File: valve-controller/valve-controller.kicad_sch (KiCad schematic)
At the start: 1 part

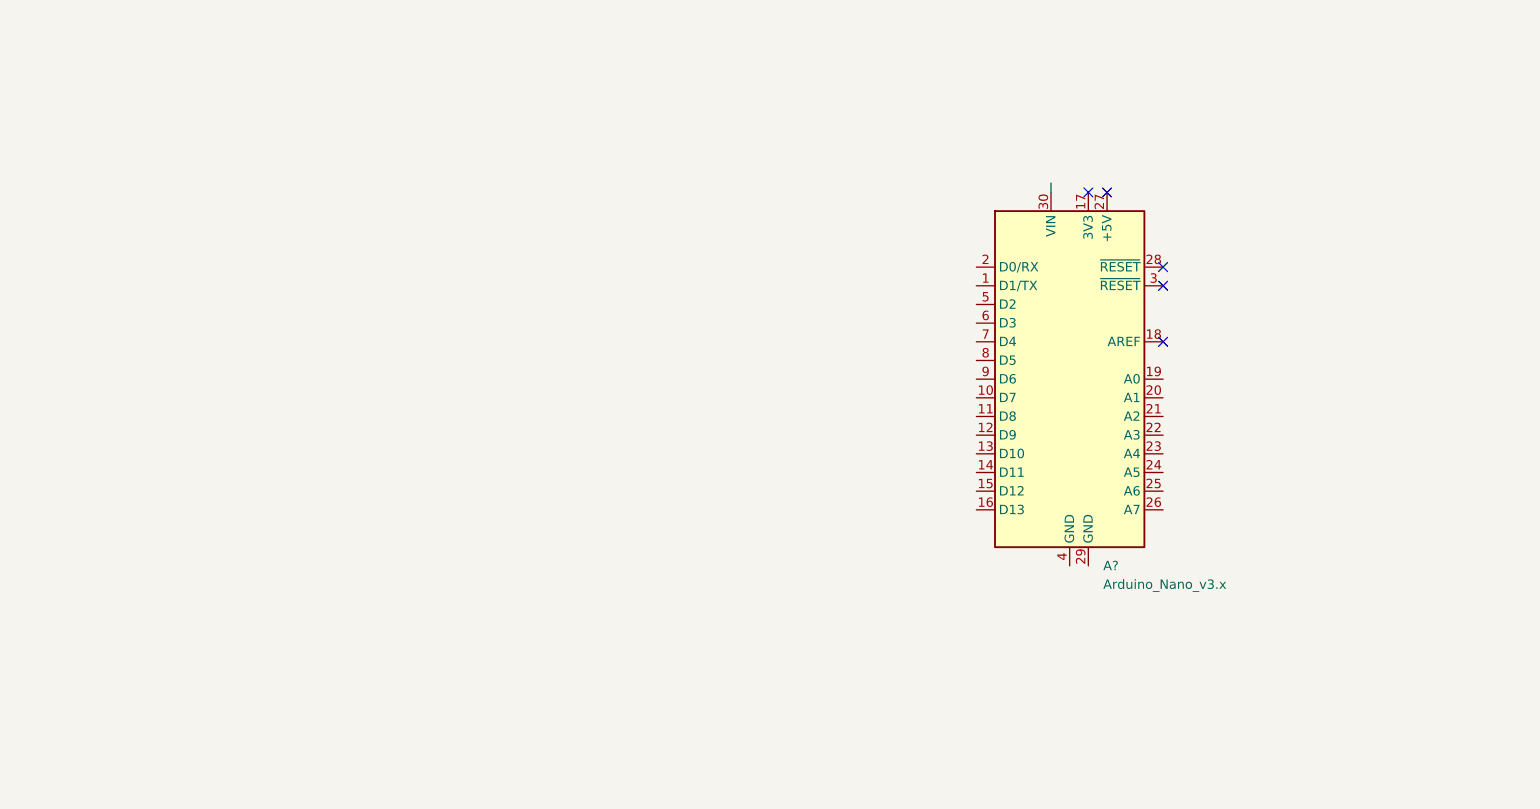
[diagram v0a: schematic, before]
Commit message: making wiring diagram for valve controller
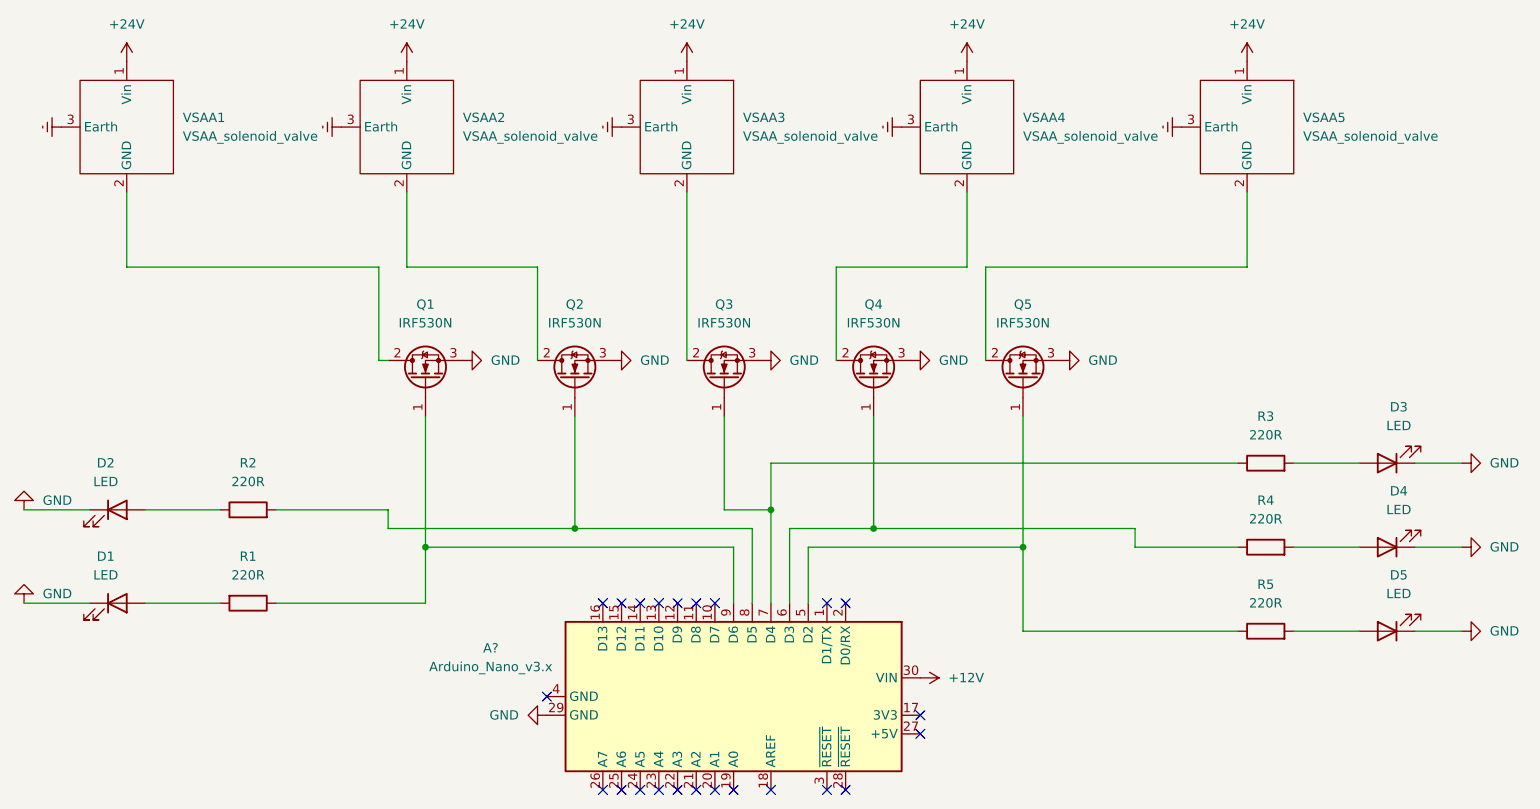
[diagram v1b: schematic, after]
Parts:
- added D1, D2, D3, D4, D5: LED, symbol Device:LED
- added Q1, Q2, Q3, Q4, Q5: IRF530N, symbol Transistor_FET:IRF540N
- added R1, R2, R3, R4, R5: 220R, symbol Device:R
- added VSAA1, VSAA2, VSAA3, VSAA4, VSAA5: VSAA_solenoid_valve, symbol my_library:VSAA_solenoid_valve
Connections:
- net GND: now reaches A?.29 (GND)
- net GND: now also D1.1 (K), D2.1 (K), D3.1 (K), D4.1 (K), D5.1 (K), Q1.3 (S), Q2.3 (S), Q3.3 (S), Q4.3 (S), Q5.3 (S)
- net +12V: now reaches A?.30 (VIN)
- net at A?.5 (D2): now also Q5.1 (G), R5.1
- net at A?.6 (D3): now also Q4.1 (G), R4.1
- net at A?.7 (D4): now also Q3.1 (G), R3.1
- net at A?.8 (D5): now also Q2.1 (G), R2.2
- net at A?.9 (D6): now also Q1.1 (G), R1.1
- new net: Q2.2 (D), VSAA2.2 (GND)
- new net: D5.2 (A), R5.2
- new net: D4.2 (A), R4.2
- new net: Q1.2 (D), VSAA1.2 (GND)
- new net: D1.2 (A), R1.2
- new net: Q3.2 (D), VSAA3.2 (GND)
- new net: D3.2 (A), R3.2
- new net: Q5.2 (D), VSAA5.2 (GND)
- new net: D2.2 (A), R2.1
- new net: Q4.2 (D), VSAA4.2 (GND)
- new net +24V: VSAA1.1 (Vin), VSAA2.1 (Vin), VSAA3.1 (Vin), VSAA4.1 (Vin), VSAA5.1 (Vin)
- new net Earth: VSAA1.3 (Earth), VSAA2.3 (Earth), VSAA3.3 (Earth), VSAA4.3 (Earth), VSAA5.3 (Earth)
- no-connect marks 5 -> 23
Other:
- title: (none) -> Valve controller
- moved on the sheet: A?

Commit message: change valves and transistors order
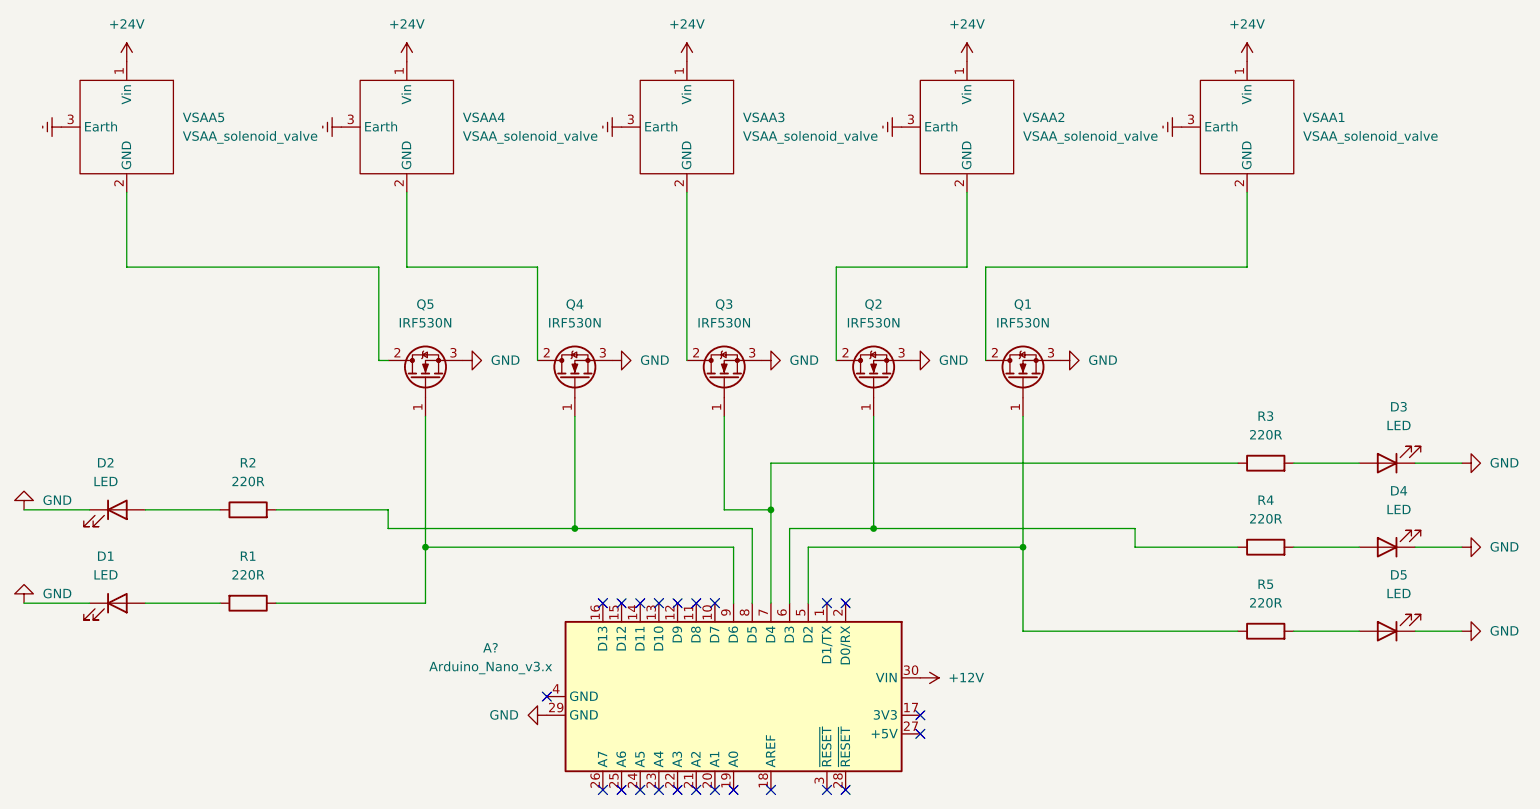
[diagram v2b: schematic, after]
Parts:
- renumbered Q5 to Q1, Q4 to Q2, Q2 to Q4, Q1 to Q5, VSAA5 to VSAA1, VSAA4 to VSAA2, VSAA2 to VSAA4, VSAA1 to VSAA5
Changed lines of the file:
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@@
   (symbol (lib_id "my_library:VSAA_solenoid_valve") (at 104.14 57.15 270) (unit 1)
     (in_bom yes) (on_board yes) (fields_autoplaced)
-    (property "Reference" "VSAA2" (id 0) (at 111.76 55.8799 90)
+    (property "Reference" "VSAA4" (id 0) (at 111.76 55.8799 90)
       (effects (font (size 1.27 1.27)) (justify left))
     )
@@
   (symbol (lib_id "Transistor_FET:IRF540N") (at 106.68 91.44 90) (unit 1)
     (in_bom yes) (on_board yes) (fields_autoplaced)
-    (property "Reference" "Q1" (id 0) (at 106.68 81.28 90))
+    (property "Reference" "Q5" (id 0) (at 106.68 81.28 90))
     (property "Value" "IRF530N" (id 1) (at 106.68 83.82 90))
     (property "Footprint" "" (id 2) (at 108.585 85.09 0)
@@
   (symbol (lib_id "Transistor_FET:IRF540N") (at 187.96 91.44 90) (unit 1)
     (in_bom yes) (on_board yes) (fields_autoplaced)
-    (property "Reference" "Q5" (id 0) (at 187.96 81.28 90))
+    (property "Reference" "Q1" (id 0) (at 187.96 81.28 90))
     (property "Value" "IRF530N" (id 1) (at 187.96 83.82 90))
     (property "Footprint" "" (id 2) (at 189.865 85.09 0)
@@
   (symbol (lib_id "my_library:VSAA_solenoid_valve") (at 66.04 57.15 270) (unit 1)
     (in_bom yes) (on_board yes) (fields_autoplaced)
-    (property "Reference" "VSAA1" (id 0) (at 73.66 55.8799 90)
+    (property "Reference" "VSAA5" (id 0) (at 73.66 55.8799 90)
       (effects (font (size 1.27 1.27)) (justify left))
     )
@@
   (symbol (lib_id "my_library:VSAA_solenoid_valve") (at 218.44 57.15 270) (unit 1)
     (in_bom yes) (on_board yes) (fields_autoplaced)
-    (property "Reference" "VSAA5" (id 0) (at 226.06 55.8799 90)
+    (property "Reference" "VSAA1" (id 0) (at 226.06 55.8799 90)
       (effects (font (size 1.27 1.27)) (justify left))
     )
@@
   (symbol (lib_id "my_library:VSAA_solenoid_valve") (at 180.34 57.15 270) (unit 1)
     (in_bom yes) (on_board yes) (fields_autoplaced)
-    (property "Reference" "VSAA4" (id 0) (at 187.96 55.8799 90)
+    (property "Reference" "VSAA2" (id 0) (at 187.96 55.8799 90)
       (effects (font (size 1.27 1.27)) (justify left))
     )
@@
   (symbol (lib_id "Transistor_FET:IRF540N") (at 127 91.44 90) (unit 1)
     (in_bom yes) (on_board yes) (fields_autoplaced)
-    (property "Reference" "Q2" (id 0) (at 127 81.28 90))
+    (property "Reference" "Q4" (id 0) (at 127 81.28 90))
     (property "Value" "IRF530N" (id 1) (at 127 83.82 90))
     (property "Footprint" "" (id 2) (at 128.905 85.09 0)
@@
   (symbol (lib_id "Transistor_FET:IRF540N") (at 167.64 91.44 90) (unit 1)
     (in_bom yes) (on_board yes) (fields_autoplaced)
-    (property "Reference" "Q4" (id 0) (at 167.64 81.28 90))
+    (property "Reference" "Q2" (id 0) (at 167.64 81.28 90))
     (property "Value" "IRF530N" (id 1) (at 167.64 83.82 90))
     (property "Footprint" "" (id 2) (at 169.545 85.09 0)
@@
       (reference "D5") (unit 1) (value "LED") (footprint "")
     )
-    (path "/1af4c67a-c000-4054-9b8f-ffb2d0e44f70"
+    (path "/9bc83bcc-e0b8-4105-9061-2c6d0758e3b7"
       (reference "Q1") (unit 1) (value "IRF530N") (footprint "")
     )
-    (path "/e3f7b2b1-9086-4943-bca4-ed77cb19a3fe"
+    (path "/e5157e2c-6aed-4c9a-ba37-76b5bf465b5a"
       (reference "Q2") (unit 1) (value "IRF530N") (footprint "")
     )
@@
       (reference "Q3") (unit 1) (value "IRF530N") (footprint "")
     )
-    (path "/e5157e2c-6aed-4c9a-ba37-76b5bf465b5a"
+    (path "/e3f7b2b1-9086-4943-bca4-ed77cb19a3fe"
       (reference "Q4") (unit 1) (value "IRF530N") (footprint "")
     )
-    (path "/9bc83bcc-e0b8-4105-9061-2c6d0758e3b7"
+    (path "/1af4c67a-c000-4054-9b8f-ffb2d0e44f70"
       (reference "Q5") (unit 1) (value "IRF530N") (footprint "")
     )
@@
       (reference "R5") (unit 1) (value "220R") (footprint "")
     )
-    (path "/b6927a09-a2f9-4c72-8b2d-0ddfde6db60a"
+    (path "/bb0bd072-604b-4f94-b7a8-ba7be997d4aa"
       (reference "VSAA1") (unit 1) (value "VSAA_solenoid_valve") (footprint "")
     )
-    (path "/05de500d-1161-4310-8519-b2804cb3777b"
+    (path "/db5ca4ae-4770-4ea2-82b0-b4805117d6f8"
       (reference "VSAA2") (unit 1) (value "VSAA_solenoid_valve") (footprint "")
     )
@@
       (reference "VSAA3") (unit 1) (value "VSAA_solenoid_valve") (footprint "")
     )
-    (path "/db5ca4ae-4770-4ea2-82b0-b4805117d6f8"
+    (path "/05de500d-1161-4310-8519-b2804cb3777b"
       (reference "VSAA4") (unit 1) (value "VSAA_solenoid_valve") (footprint "")
     )
-    (path "/bb0bd072-604b-4f94-b7a8-ba7be997d4aa"
+    (path "/b6927a09-a2f9-4c72-8b2d-0ddfde6db60a"
       (reference "VSAA5") (unit 1) (value "VSAA_solenoid_valve") (footprint "")
     )
